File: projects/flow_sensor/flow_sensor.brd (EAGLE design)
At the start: 39.4 x 49.5 mm, 90 parts, among them IC1 TPS61200, IC2 TPS61200, IC3 MIC5219BM5, J5 455-1750-1-ND

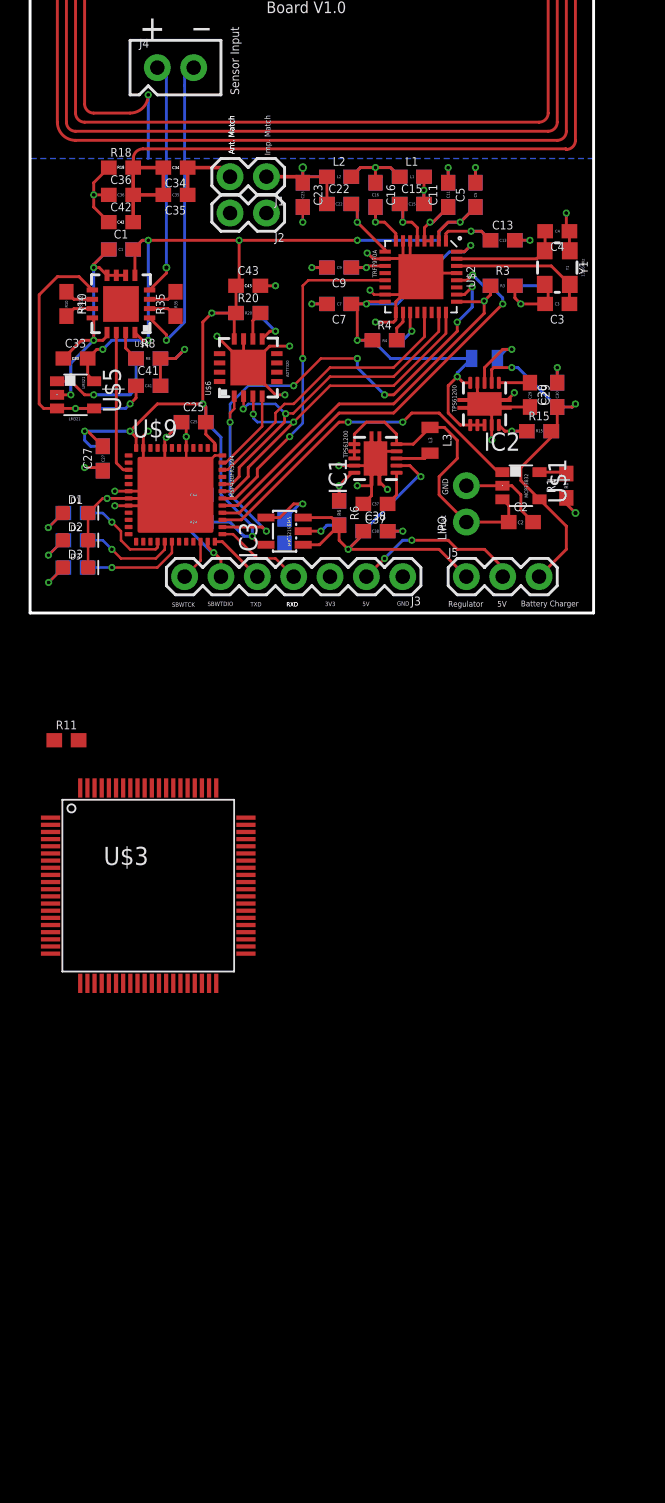
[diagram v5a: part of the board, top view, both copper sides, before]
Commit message: Added MAX1726 linear regulator and replaced circuit-side boost converter
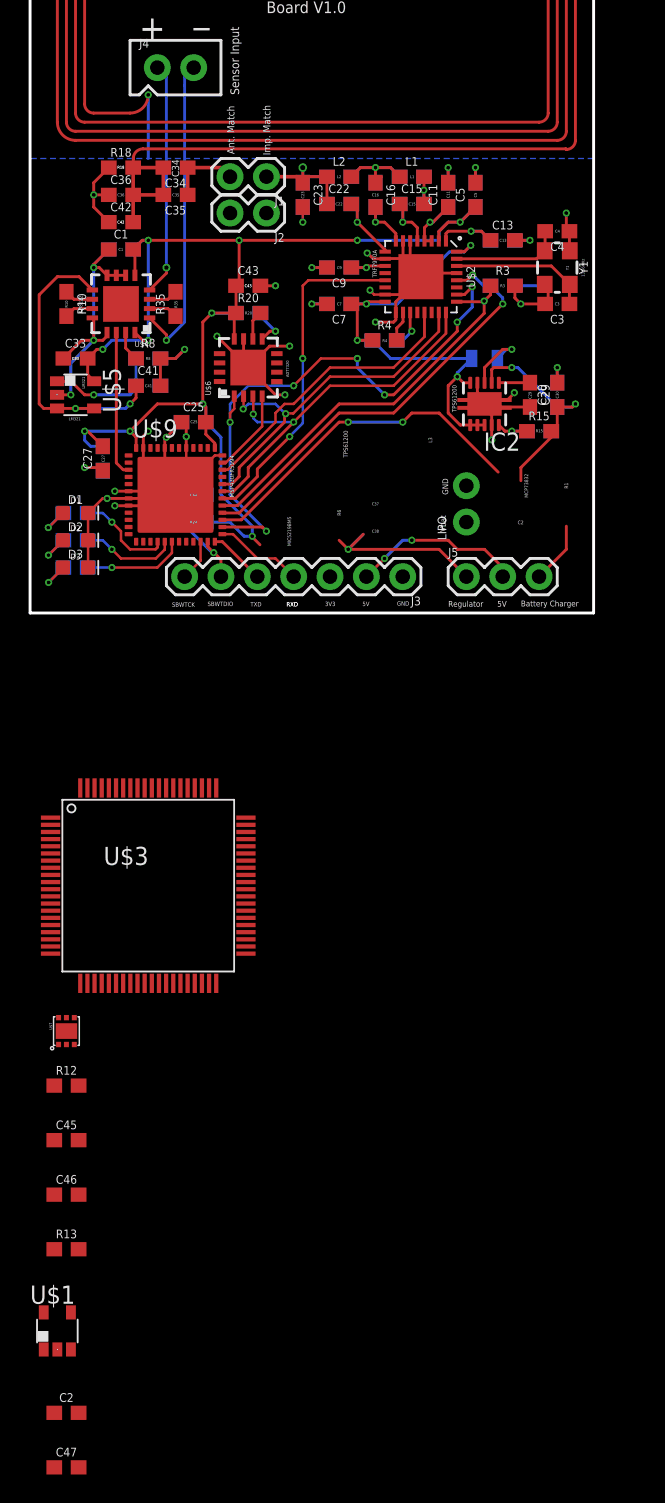
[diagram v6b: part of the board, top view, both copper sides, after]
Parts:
- removed C37: 0.1uF, SparkFun-Capacitors:0603
- removed C38, C39: 10uF, SparkFun-Capacitors:0603
- removed IC1: TPS61200, texas:S-PDSO-N10
- removed IC3: MIC5219BM5, v-reg-micrel:SOT23-5
- removed L3: 2.2µH, SparkFun-Coils:0805
- removed R1: 67k, SparkFun-Resistors:0603
- removed R11, R7: 180k, SparkFun-Resistors:0603
- removed R17: 300k, SparkFun-Resistors:0603
- removed R6: 1.2M, SparkFun-Resistors:0603
- added C45, C46, C47: 1uF, SparkFun-Capacitors:0603
- added R12: 27k, SparkFun-Resistors:0603
- added R13: 56k, SparkFun-Resistors:0603
- added U$7: XC6805, my_library:DFN6-1.8X2.0
- C2: value 4.7uF -> 1uF
- U$1: value MCP73832 -> MAX1726
- moved C2 69.9 mm to (2.54, -55.9)
- moved U$1 67.4 mm to (1.91, -50.2), turned to 0 degrees
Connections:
- removed net N$17: IC1.10, R6.1, R7.2
- removed net N$2: R1.2, U$1.5
- removed net N$20: IC1.3, L3.2
- removed net N$25: IC3.4, R17.2
- removed net N$3: C37.1, IC1.1
- removed net N$30: C38.1, C39.1, IC1.2, IC3.1, IC3.3, J5.1, R6.2
- new net N$39: R12.2, U$7.4
- net CHG_STAT: now also R13.2, U$7.3; no longer U$1.1
- net GND: now also C2.1, C45.1, C46.1, C47.1, R12.1, U$1.4, U$7.2, U$7.PAD; no longer C2.2, C37.2, C38.2, C39.2, IC1.4, IC1.9, IC1.PP, IC1.PP@1, IC1.PP@2, IC3.2, R1.1, R17.1, R7.1
- net VBAT: now also C2.2, C45.2, J5.1, U$1.1, U$1.5, U$7.1; no longer C2.1, IC1.5, IC1.6, IC1.7, IC1.8, L3.1, U$1.3
- net VCC: now also C47.2, U$1.3; no longer IC3.5
- net VCHGR: now also C46.2, R13.1, U$7.6; no longer U$1.4
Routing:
- net N$30: track 29.7 -> 0.00 mm, vias 2 -> 0
- net GND: track 556.0 -> 532.0 mm, vias 36 -> 30
- net VBAT: track 22.9 -> 13.8 mm, vias 0 -> 1
- net N$25: track 4.67 -> 0.00 mm, vias 1 -> 0
- net VCHGR: track 24.4 -> 19.9 mm
- net N$17: track 3.55 -> 0.00 mm, vias 1 -> 0
- net N$20: track 2.49 -> 0.00 mm
- net N$3: track 2.43 -> 0.00 mm
- net N$2: track 1.92 -> 0.00 mm

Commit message: Added LTC1517-5 charge pump to replace battery-site boost converter
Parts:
- removed C29: 0.1uF, SparkFun-Capacitors:0603
- removed C30, C31: 10uF, SparkFun-Capacitors:0603
- removed IC2: TPS61200, texas:S-PDSO-N10
- removed L4: 2.2µH, SparkFun-Coils:0805
- removed R15: 1.6M, SparkFun-Resistors:0603
- removed R16: 200k, SparkFun-Resistors:0603
- added C37: 0.1uF, SparkFun-Capacitors:0603
- added U$8: LTC1517-5, my_library:SOT-23-5
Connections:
- removed net N$1: IC2.3, L4.2
- removed net N$18: C29.1, IC2.1
- removed net N$22: IC2.10, R15.1, R16.2
- new net N$2: C37.1, U$8.5
- new net N$3: C37.2, U$8.4
- net GND: now also U$8.2; no longer C29.2, C30.2, C31.2, IC2.4, IC2.9, IC2.PP, IC2.PP@1, IC2.PP@2, R16.1
- net VCHGR: now also U$8.3; no longer C30.1, C31.1, IC2.2, R15.2
- net VIN: now also U$8.1; no longer IC2.5, IC2.6, IC2.7, IC2.8, L4.1
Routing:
- net VCHGR: track 19.9 -> 4.31 mm, vias 2 -> 0
- net VIN: track 34.4 -> 20.2 mm, vias 4 -> 3
- net GND: track 532.0 -> 519.9 mm, vias 30 -> 27
- net N$1: track 4.76 -> 0.00 mm, vias 1 -> 0
- net N$22: track 3.19 -> 0.00 mm, vias 1 -> 0
- net N$18: track 2.18 -> 0.00 mm

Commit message: Added RM25C256C EEPROM for external data storage
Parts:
- added C29: 0.1uF, SparkFun-Capacitors:0603
- added U$10: RM25C256C, my_library:DFN8-2X3
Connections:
- removed net SCLK: U$2.26, U$6.1, U$9.26
- new net SCK: U$10.6, U$2.26, U$6.1, U$9.26
- net GND: now also C29.2, U$10.4
- net MISO: now also U$10.2
- net MOSI: now also U$10.5
- net VCC: now also C29.1, U$10.8
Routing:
- net SCLK: track 40.4 -> 0.00 mm, vias 7 -> 0
- net SCK: track 0.00 -> 40.4 mm, vias 0 -> 7
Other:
- board text removed: "C2"
- board text removed: "C29"
- board text removed: "C30"
- board text removed: "C31"
- board text removed: "C37"
- board text removed: "C38"
- board text removed: "C39"
- board text removed: "L3"
- board text removed: "L4"
- board text removed: "MCP73832"
- board text removed: "R1"
- board text removed: "R15"
- board text removed: "R16"
- board text removed: "R6"
- board text removed: "R7"
